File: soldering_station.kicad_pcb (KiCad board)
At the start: 2 copper layers, 121 x 38.4 mm, 71 parts, among them IC1 ATMEGA8A-P, P1 17v, P2 220v, P3 24v|220v, P4 solder, P5 thermocouple, P6 Fan, P7 thermocouple, P8 Heater, Q1 КТ313Б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

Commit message: Fix board
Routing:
- net (no net): track 55.0 -> 26.2 mm
- net GND: track 539.3 -> 544.8 mm

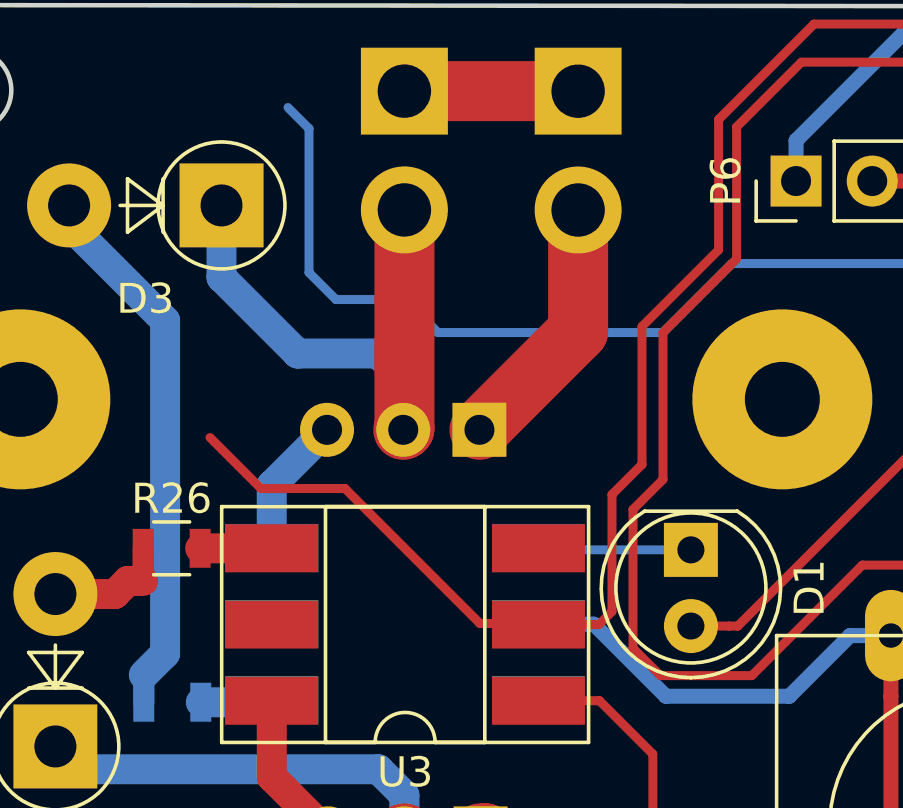
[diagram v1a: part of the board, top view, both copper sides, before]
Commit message: Add PCB PDFs
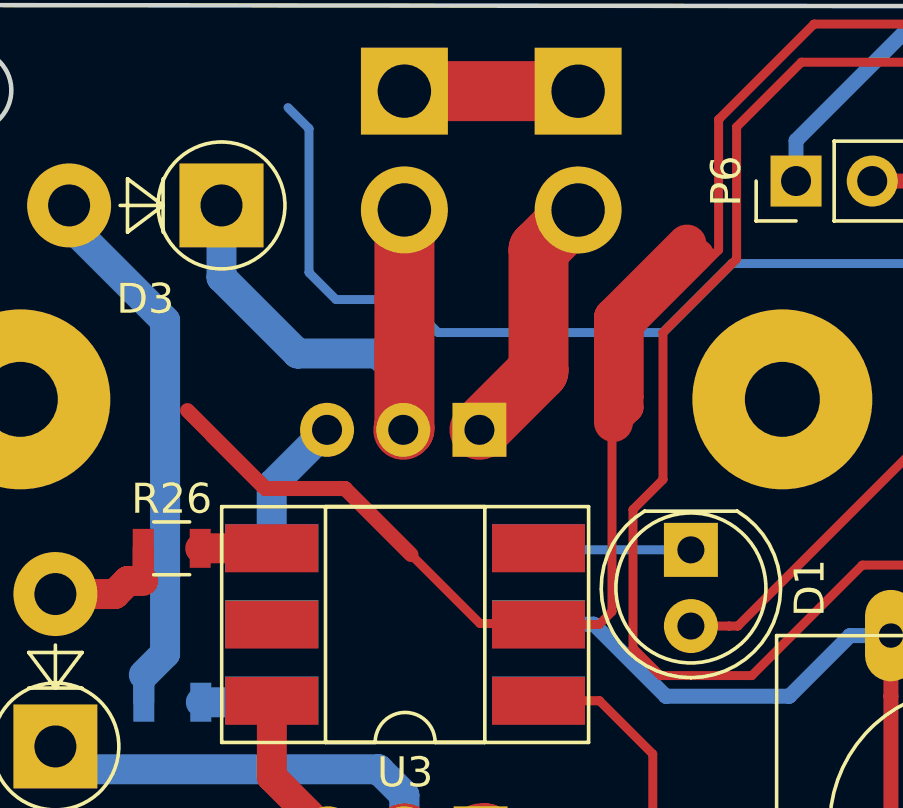
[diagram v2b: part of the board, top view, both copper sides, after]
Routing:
- net GND: track 544.8 -> 564.9 mm

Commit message: Add connectors
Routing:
- net GND: track 564.9 -> 558.0 mm
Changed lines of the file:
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@@
     (thickness 1.6)
     (drawings 10)
-    (tracks 763)
+    (tracks 762)
     (zones 0)
     (modules 71)
@@
   )
   (setup
-    (last_trace_width 1.3)
+    (last_trace_width 0.3)
     (user_trace_width 0.25)
     (user_trace_width 0.3)
@@
   (segment (start 148.4 52.45) (end 148.25 52.45) (width 0.25) (layer B.Cu) (net 1))
   (segment (start 149.35 53.55) (end 149.35 53.4) (width 0.25) (layer B.Cu) (net 1))
-  (segment (start 171.704 68.727) (end 164.814814 68.727) (width 0.25) (layer B.Cu) (net 1))
   (segment (start 132.25 48.45) (end 132.2 48.4) (width 0.25) (layer B.Cu) (net 1))
   (segment (start 149.35 53.4) (end 148.4 52.45) (width 0.25) (layer B.Cu) (net 1))

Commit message: Display PCB
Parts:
- removed D3, D4: 1N4007, Diodes_THT:D_5W_P5.08mm_Vertical_AnodeUp
- removed REF**: Heatsink_Fischer_SK104-STC-STIC_35x13mm_2xDrill2.5mm, Heatsinks:Heatsink_Fischer_SK104-STC-STIC_35x13mm_2xDrill2.5mm
- removed SW1: mode, Buttons_Switches_THT:SW_PUSH-12mm
- added K1: dec in, Connector_PinHeader_2.54mm:PinHeader_1x03_P2.54mm_Vertical, F.Cu at (268.9, 140.6)
- added K2: dec out, Connector_PinHeader_2.54mm:PinHeader_1x03_P2.54mm_Vertical, F.Cu at (206.2, 59.9)
- added P10: disp in, Connector_PinHeader_2.54mm:PinHeader_1x07_P2.54mm_Vertical, F.Cu at (231.5, 127.9)
- added P9: disp out, Connector_PinHeader_2.54mm:PinHeader_1x07_P2.54mm_Vertical, F.Cu at (206.3, 83.9)
- BZ1: footprint Buzzers_Beepers:Buzzer_12x9.5RM7.6 -> Buzzer_Beeper:Buzzer_12x9.5RM7.6; moved to F.Cu
- C1, C2, C7, C9: footprint Capacitors_SMD:C_0805 -> Capacitor_SMD:C_0805_2012Metric; moved to F.Cu
- C3: footprint Capacitors_ThroughHole:CP_Radial_D8.0mm_P3.80mm -> Capacitor_THT:CP_Radial_D8.0mm_P3.80mm; moved to F.Cu
- C4, C5, C8: footprint Capacitors_SMD:C_0805 -> Capacitor_SMD:C_0805_2012Metric
- C6: footprint Capacitors_ThroughHole:CP_Radial_D5.0mm_P2.50mm -> Capacitor_THT:CP_Radial_D5.0mm_P2.50mm; moved to F.Cu
- D1, D2: footprint LEDs:LED_D5.0mm -> LED_THT:LED_D5.0mm
- D5: footprint Oscillators:Oscillator_SMD_SeikoEpson_SG8002JA-4pin_14.0x8.7mm -> Oscillator:Oscillator_SMD_SeikoEpson_SG8002JA-4Pin_14.0x8.7mm
- HG1: footprint Displays_7-Segment:MAN3640A -> lib:иб
- HG2, HG3: footprint Housings_DIP:DIP-14_W7.62mm_LongPads -> Package_DIP:DIP-14_W7.62mm
- IC1: footprint Housings_DIP:DIP-28_W7.62mm_LongPads -> Package_DIP:DIP-28_W7.62mm_LongPads
- P1, P5, P6, SB1: footprint Pin_Headers:Pin_Header_Straight_1x02_Pitch2.54mm -> Connector_PinHeader_2.54mm:PinHeader_1x02_P2.54mm_Vertical
- P2, P3, P4, P8: footprint Pin_Headers:Pin_Header_Straight_1x02_Pitch3.96mm_Friction_Lock -> Connector_Wire:SolderWirePad_1x02_P5.08mm_Drill1.5mm; moved to F.Cu
- P7: footprint Pin_Headers:Pin_Header_Straight_1x03_Pitch2.54mm -> Connector_PinHeader_2.54mm:PinHeader_1x03_P2.54mm_Vertical
- Q1, Q2: footprint TO_SOT_Packages_THT:TO-92_Molded_Wide_Oval -> Package_TO_SOT_THT:TO-92L_Wide
- Q3: footprint TO_SOT_Packages_THT:TO-92_Molded_Wide_Oval -> Package_TO_SOT_THT:TO-92_Wide
- Q4: footprint TO_SOT_Packages_THT:TO-126_Vertical -> Package_TO_SOT_THT:TO-126-3_Vertical; moved to F.Cu
- R1, R16, R18: footprint Resistors_SMD:R_0805 -> Resistor_SMD:R_0805_2012Metric; moved to F.Cu
- R10, R11, R12, R13, R14, R15, R17, R19, R2, R20, R21, R22, R23, R24, R27, R28, R3, R4, R5, R6, R7, R8: footprint Resistors_SMD:R_0805 -> Resistor_SMD:R_0805_2012Metric
- R25, R26: value 360 -> 270; footprint Resistors_SMD:R_0805 -> Resistor_SMD:R_0805_2012Metric
- R9: footprint Resistors_SMD:R_0805 -> Resistor_SMD:R_0805_2012Metric; moved to B.Cu
- RV1, RV2: footprint Potentiometers:Potentiometer_Trimmer_ACP_CA9v_Horizontal_Px10.0mm_Py5.0mm -> Potentiometer_THT:Potentiometer_ACP_CA9-V10_Vertical; moved to F.Cu
- SW2: footprint lib:Encoder_with_button -> Connector_PinHeader_2.54mm:PinHeader_1x05_P2.54mm_Vertical
- U1: footprint Housings_DIP:DIP-8_W8.89mm_SMDSocket_LongPads -> Package_DIP:DIP-8_W8.89mm_SMDSocket_LongPads
- U2, U3: footprint Housings_DIP:DIP-6_W8.89mm_SMDSocket_LongPads -> Package_DIP:DIP-6_W8.89mm_SMDSocket_LongPads
- U4: footprint Power_Integrations:TO-220 -> Package_TO_SOT_THT:TO-220-3_Vertical; moved to F.Cu
- VD1, VD2: value BT139 -> BT136; footprint TO_SOT_Packages_THT:TO-220_Vertical -> Package_TO_SOT_THT:TO-220-3_Vertical; moved to F.Cu
- moved R4 157.7 mm to (242.9, 136.8), turned to 90 degrees
- moved HG3 147.8 mm to (258.0, 127.9)
- moved R6 147.7 mm to (237.8, 142.3)
- moved HG2 147.1 mm to (246.6, 127.9)
- moved R5 147.0 mm to (240.1, 142.4), turned to 90 degrees
- moved R3 146.9 mm to (239.8, 129.0)
- moved HG1 146.5 mm to (239.0, 135.5)
- moved R2 146.3 mm to (239.8, 126.5)
- moved R7 138.9 mm to (249.1, 131.7), turned to 270 degrees
- moved C4 130.4 mm to (37.3, 124.9), turned to 0 degrees
- moved C7 130.2 mm to (39.0, 152.3)
- moved C1 129.9 mm to (198.8, 152.4)
- moved R8 129.6 mm to (239.8, 132.6), turned to 180 degrees
- moved P6 121.8 mm to (206.2, 87.5), turned to 0 degrees
- moved R28 121.4 mm to (86.1, 151.0), turned to 0 degrees
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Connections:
- P2 pad 2: Net-(D3-Pad1) -> Net-(P2-Pad2)
- P3 pad 2: Net-(D4-Pad1) -> Net-(P3-Pad2)
- Q1 pad 1: Net-(HG1-Pad4) -> Net-(K2-Pad3)
- Q2 pad 1: Net-(HG2-Pad9) -> Net-(K2-Pad2)
- Q3 pad 1: Net-(HG3-Pad9) -> Net-(K2-Pad1)
- R2 pad 2: Net-(IC1-Pad2) -> Net-(P10-Pad1)
- R25 pad 1: Net-(D3-Pad2) -> Net-(P2-Pad2)
- R26 pad 1: Net-(D4-Pad2) -> Net-(P3-Pad2)
- R3 pad 2: Net-(IC1-Pad3) -> Net-(P10-Pad2)
- R4 pad 2: Net-(IC1-Pad4) -> Net-(P10-Pad3)
- R5 pad 2: Net-(IC1-Pad5) -> Net-(P10-Pad4)
- R6 pad 2: Net-(IC1-Pad6) -> Net-(P10-Pad5)
- R7 pad 2: Net-(IC1-Pad11) -> Net-(P10-Pad6)
- R8 pad 2: Net-(IC1-Pad12) -> Net-(P10-Pad7)
- SW2 pad 5: GND -> Net-(IC1-Pad28)
- VD1 pad 1: Net-(P8-Pad2) -> Net-(P2-Pad2)
- VD1 pad 2: Net-(D3-Pad1) -> Net-(P8-Pad2)
- VD2 pad 1: Net-(P4-Pad2) -> Net-(P3-Pad2)
- VD2 pad 2: Net-(D4-Pad1) -> Net-(P4-Pad2)
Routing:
- net GND: track 558.0 -> 0.00 mm
- net +5V: track 257.9 -> 0.00 mm, vias 1 -> 0
- net Net-(IC1-Pad25): track 130.8 -> 0.00 mm
- net Net-(IC1-Pad27): track 89.1 -> 0.00 mm
- net Net-(IC1-Pad26): track 86.7 -> 0.00 mm
- net +24V: track 81.5 -> 0.00 mm
- net Net-(IC1-Pad19): track 62.8 -> 0.00 mm
- net Net-(R16-Pad1): track 62.2 -> 0.00 mm
- net Net-(R15-Pad1): track 59.9 -> 0.00 mm
- net Net-(IC1-Pad13): track 49.0 -> 0.00 mm
- net Net-(HG1-Pad4): track 88.7 -> 40.0 mm
- net Net-(P7-Pad1): track 40.7 -> 0.00 mm
- net Net-(IC1-Pad18): track 39.3 -> 0.00 mm
- net Net-(IC1-Pad17): track 38.6 -> 0.00 mm
- net Net-(IC1-Pad6): track 38.1 -> 0.00 mm
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- added copper zone on B.Cu, net (none)
- removed copper zone on B.Cu, net GND
- removed copper zone on F.Cu, net GND
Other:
- board size 121 x 38.4 mm -> 42.4 x 23 mm
- board text added: "Display"

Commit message: Display PCB
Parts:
- moved BZ1 14.9 mm to (165.3, 27.6)
- moved R10 7.68 mm to (196.7, 65.1)
- moved Q1 6.49 mm to (203.0, 64.3)
- moved Q2 6.49 mm to (203.0, 58.9)
- moved Q3 6.49 mm to (203.0, 53.4)
- moved P5 5.58 mm to (210.2, 12.6)
- moved P7 5.58 mm to (202.1, 14.2)
- moved RV2 5.58 mm to (182.8, 26.1)
- moved RV1 5.58 mm to (199.5, 34.0)
- moved SB1 5.35 mm to (207.4, 105.6)
- moved K2 4.52 mm to (207.5, 55.6)
- moved P6 4.52 mm to (207.4, 83.1)
- moved P9 4.52 mm to (207.5, 79.5)
- moved SW2 4.52 mm to (207.5, 99.5)
- moved P4 4.38 mm to (161.9, 80.4)
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
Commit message: Update PCB
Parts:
- C1, C2, C4, C5, C7, C8, C9, D5, R1, R11, R14, R15, R16, R17, R18, R19, R20, R21, R22, R23, R24, R27, R28, U1: moved to B.Cu
- moved C7 176.8 mm to (193.0, 65.5), turned to 90 degrees
- moved C4 171.1 mm to (182.4, 34.4), turned to 90 degrees
- moved R28 169.4 mm to (203.6, 29.0), turned to 180 degrees
- moved C5 169.3 mm to (197.6, 31.9), turned to 90 degrees
- moved C8 162.3 mm to (191.1, 29.3), turned to 90 degrees
- moved R23 144.8 mm to (180.1, 34.4), turned to 270 degrees
- moved R19 136.8 mm to (181.7, 37.9)
- moved R22 132.3 mm to (194.3, 29.3), turned to 90 degrees
- moved C2 130.8 mm to (192.3, 44.0), turned to 90 degrees
- moved R24 123.4 mm to (199.9, 31.9), turned to 270 degrees
- moved R27 118.7 mm to (176.3, 29.0)
- moved R15 117.5 mm to (184.7, 44.0), turned to 270 degrees
- moved R11 116.1 mm to (186.1, 54.1), turned to 180 degrees
- moved R1 112.3 mm to (187.7, 81.3), turned to 90 degrees
- moved R21 112.0 mm to (198.4, 35.3), turned to 180 degrees
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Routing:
- net +5V: track 0.00 -> 108.8 mm
- net GND: track 0.00 -> 46.5 mm
- net Net-(R25-Pad2): track 0.00 -> 25.9 mm
- net Net-(R16-Pad1): track 0.00 -> 22.2 mm
- net Net-(R19-Pad1): track 0.00 -> 18.6 mm
- net Net-(U3-Pad6): track 0.00 -> 18.4 mm
- net Net-(P8-Pad2): track 0.00 -> 16.3 mm
- net Net-(P3-Pad2): track 0.00 -> 15.7 mm
- net Net-(R19-Pad2): track 0.00 -> 13.1 mm
- net Net-(R21-Pad1): track 0.00 -> 12.7 mm
- net Net-(R21-Pad2): track 0.00 -> 11.8 mm
- net Net-(P2-Pad2): track 0.00 -> 11.3 mm
- net Net-(P4-Pad2): track 0.00 -> 10.4 mm
- net Net-(R26-Pad2): track 0.00 -> 9.94 mm
- net Net-(U2-Pad6): track 0.00 -> 9.34 mm
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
